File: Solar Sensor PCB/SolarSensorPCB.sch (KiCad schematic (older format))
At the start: 36 parts, among them J1 Arduino_Nano_Header, P1 BATT, P10 SERIAL, P2 BATT, P3 DIO, P4 LOGO1, P5 LOGO2, P6 PCB, P7 ENC, P8 AREF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

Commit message: Updated PCB. Not finished yet!
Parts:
- removed BT1: PP3, symbol device:Battery
- removed C2: 100u, REInnovationFootprint:C_1V7_TH, symbol device:CP1
- removed C3: 100n, matts_components:C1_wide_lg_pad, symbol device:C
- removed D1: 1N5819, REInnovationFootprint:TH_Diode_1, symbol device:D_Schottky
- removed DISP1: OLED_I2C, REInnovationFootprint:TH_OLED1306, symbol SolarSensorPCB-rescue:OLED_I2C-matts_components
- removed J1: Arduino_Nano_Header, REInnovationFootprint:NANO_DIP_30_600, symbol SolarSensorPCB-rescue:Arduino_Nano_Header-matts_components
- removed P1: BATT, symbol Connector_Generic:Conn_01x02
- removed P2: BATT, REInnovationFootprint:Batt_Connector_Strain_Relief, symbol Connector_Generic:Conn_01x02
- removed P3: DIO, matts_components:SIL-8_lg_pad_1mm, symbol Connector_Generic:Conn_01x08
- removed P8: AREF, matts_components:SIL-2_solder_connect, symbol Connector_Generic:Conn_01x02
- removed P9: AIO, matts_components:SIL-3_lg_pad_1mm, symbol Connector_Generic:Conn_01x03
- removed R2: 4K7, REInnovationFootprint:TH_Resistor_1, symbol device:R
- removed SW2: DOWN, REInnovationFootprint:SW_PUSH_SMALL_lg_pad, symbol SolarSensorPCB-rescue:SW_PUSH-matts_components
- removed SW3: SPST, REInnovationFootprint:SW_SPDT_R_Angle_ALIEX, symbol SolarSensorPCB-rescue:SPST-matts_components
- removed U1: DS18B20, matts_components:TO92-EBC_large_pad, symbol SolarSensorPCB-rescue:DS18B20-matts_components
- removed U2: MCP1702-50, matts_components:TO92_MC1703, symbol SolarSensorPCB-rescue:MCP1702-50-matts_components
- removed U?: TLC2252A, symbol device:Opamp_Dual_Generic
- removed U?: TLC2252A, symbol Device:Opamp_Dual_Generic
- added C4: 100n, REInnovationFootprint:SM_C_0805, symbol device:C
- added D1: LED, REInnovationFootprint:SM0805_LED, symbol device:LED
- added IC1: ATTINY85-P, REInnovationFootprint:SM_SOIC_8, symbol matts_components:ATTINY85-P
- added J1: ISP, REInnovationFootprint:ISP_3x2, symbol Connector_Generic:Conn_02x03_Odd_Even
- added J2: ADC, REInnovationFootprint:SIL-4_large_pad, symbol Connector_Generic:Conn_01x04
- added P1: I2C_OLED, REInnovationFootprint:SIL-4_large_pad, symbol Connector_Generic:Conn_01x04
- added R6: 330R, REInnovationFootprint:SM0805, symbol device:R
- added U1: TSV911xxLx, REInnovationFootprint:SM_SOT-23-5, symbol Amplifier_Operational:TSV911xxLx
- added U2: LM75B, REInnovationFootprint:SM_SOIC_8, symbol Sensor_Temperature:LM75B
- C1: footprint matts_components:C1_wide_lg_pad -> REInnovationFootprint:SM_C_0805
- C2, C3, C6: renamed from C?; footprint matts_components:C1_wide_lg_pad -> REInnovationFootprint:SM_C_0805
- C5: renamed from C?; footprint REInnovationFootprint:C_1V7_TH -> REInnovationFootprint:SM_4x5.3
- P10: footprint matts_components:SIL-4_Grove_SIL -> REInnovationFootprint:SIL-4_Grove_SCREW
- P6: footprint REInnovationFootprint:PCB_50x100mm_PP3_CutOut_EdgeCut -> REInnovationFootprint:PCB_50x50mm_PP3_Cutout
- R1, R2, R3, R5: renamed from R?; footprint (none) -> REInnovationFootprint:SM0805
- R4: value 100k -> 47k; footprint REInnovationFootprint:TH_Resistor_1 -> REInnovationFootprint:SM0805
- U3: renamed from U?; footprint (none) -> REInnovationFootprint:SM_MSOP10-0.5
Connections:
- net labels added: D0, D1, D2, D3, D4, IRR1+, IRR1-, SW1
- net labels removed: IRR, IRR+, IRR-, SW_DOWN, SW_UP, TEMP_DATA, VCC
- wire segments 163 -> 140
- no-connect marks 8 -> 5
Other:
- note added: "ATTiny85 Arduino Pins:\nIC Pin: Arduino Ref\n1 5/A0/RST\n2 3/A3\n3 4/A2\n4 GND\n5 0 - PWM\n6 1 - PWM\n7 2/A1\n8 +ve supply"
- note added: "I2C Pull Up"
- note added: "ISP Connections:\n1 - MISO\n2 - Vcc\n3 - SCLK\n4 - MOSI\n5 - Reset\n6 - GND"
- note added: "Irradiance sensor + amplifier"
- note added: "Potential OLED output for a little display?"
- note added: "Switch/LED combo for \ndata display and user input"
- note added: "We can measure two more \nanalog pins here, if needed."
- note removed: "Battery Supply. Switch on Batt Holder"
- moved on the sheet: C1, C2, C3, C5, C6, D2, P10, P4, P5, P6, P7, R1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

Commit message: Updated PCB v0.1
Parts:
- removed P4: LOGO1, CuriousElectric3:CEC_Globe_10mm_FCU, symbol Connector_Generic:Conn_01x01
- C1: JLCPCB Add (none) -> Y; JLCPCB Cost (none) -> 0.0105; LCSC (none) -> C107135
- C2, C3, C4, C6: JLCPCB Add (none) -> Y; JLCPCB Cost (none) -> 0.0108; LCSC (none) -> C49678
- C5: JLCPCB Add (none) -> Y; JLCPCB Cost (none) -> 0.0566; LCSC (none) -> C134722
- D1: JLCPCB Add (none) -> Y; JLCPCB Cost (none) -> 0.0135; LCSC (none) -> C2293
- P6: footprint REInnovationFootprint:PCB_50x50mm_PP3_Cutout -> REInnovationFootprint:PCB_40mm_Round
- R1: JLCPCB Add (none) -> Y; JLCPCB Cost (none) -> 0.0045; LCSC (none) -> C38522
- R2: JLCPCB Add (none) -> Y; JLCPCB Cost (none) -> 0.0045; LCSC (none) -> C17414
- R3: JLCPCB Add (none) -> Y; JLCPCB Cost (none) -> 0.0040; LCSC (none) -> C17414
- R4: JLCPCB Add (none) -> Y; JLCPCB Cost (none) -> 0.0040; LCSC (none) -> C17713
- R5: JLCPCB Add (none) -> Y; JLCPCB Cost (none) -> 0.0040; LCSC (none) -> C38522
- R6: JLCPCB Add (none) -> Y; JLCPCB Cost (none) -> 0.0050; LCSC (none) -> C237764
- SW1: footprint REInnovationFootprint:SW_PUSH_SMALL_lg_pad -> REInnovationFootprint:SMD_SW_6x3_5; JLCPCB Add (none) -> Y; JLCPCB Cost (none) -> 0.0391; LCSC (none) -> C319333
- U1: JLCPCB Add (none) -> Y; JLCPCB Cost (none) -> 0.4576; LCSC (none) -> C361052
- U2: JLCPCB Add (none) -> Y; JLCPCB Cost (none) -> 0.3457; LCSC (none) -> C34565
- U3: JLCPCB Add (none) -> Y; JLCPCB Cost (none) -> 4.7766; LCSC (none) -> C37593
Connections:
- net D0: now also P1.4 (Pin_4), U2.1 (SDA), U3.9 (SDA); no longer P1.3 (Pin_3), U2.2 (SCL), U3.10 (SCL)
- net D2: now also P1.3 (Pin_3), U2.2 (SCL), U3.10 (SCL); no longer P1.4 (Pin_4), U2.1 (SDA), U3.9 (SDA)
- net IRR1+: no longer names the net of C1.1, R4.1, U1.1, U3.4 (AIN0)
- no-connect marks 5 -> 4
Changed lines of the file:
@@
 F 0 "SW1" H 9550 4350 50  0000 C CNN
 F 1 "UP" H 9550 4100 50  0000 C CNN
-F 2 "REInnovationFootprint:SW_PUSH_SMALL_lg_pad" H 9550 4400 50  0001 C CNN
+F 2 "REInnovationFootprint:SMD_SW_6x3_5" H 9550 4400 50  0001 C CNN
 F 3 "" H 9550 4400 50  0000 C CNN
+F 4 "C319333" H 9550 4200 50  0001 C CNN "LCSC"
+F 5 "Y" H 9550 4200 50  0001 C CNN "JLCPCB Add"
+F 6 "0.0391" H 9550 4200 50  0001 C CNN "JLCPCB Cost"
 	1    9550 4200
 	1    0    0    -1
@@
 Text HLabel 7150 3650 2    60   Output ~ 0
 SCL_I2C
-Text HLabel 4450 4700 0    60   Input ~ 0
-IRR1+
 Text HLabel 7150 3800 2    60   Output ~ 0
 SDA_I2C
@@
 F 2 "REInnovationFootprint:SM0805" V 2280 3450 50  0001 C CNN
 F 3 "" H 2350 3450 50  0000 C CNN
+F 4 "C17713" H 2350 3450 50  0001 C CNN "LCSC"
+F 5 "Y" H 2350 3450 50  0001 C CNN "JLCPCB Add"
+F 6 "0.0040" H 2350 3450 50  0001 C CNN "JLCPCB Cost"
 	1    2350 3450
 	0    1    1    0
@@
 	-1   0    0    -1
 $EndComp
-Text HLabel 3250 2300 0    60   Input ~ 0
+Text HLabel 3250 2350 0    60   Input ~ 0
 Rx
-Text HLabel 3250 2400 0    60   Input ~ 0
+Text HLabel 3250 2450 0    60   Input ~ 0
 Tx
-Text HLabel 1500 2250 2    60   Input ~ 0
-Rx
-Text HLabel 1500 2150 2    60   Input ~ 0
-Tx
-Wire Wire Line
-	1500 2250 1250 2250
-Wire Wire Line
-	1500 2150 1250 2150
 Wire Wire Line
 	1750 2000 1750 2050
@@
 F 2 "REInnovationFootprint:SM_C_0805" H 2388 3000 50  0001 C CNN
 F 3 "" H 2350 3150 50  0000 C CNN
+F 4 "C107135" H 2350 3150 50  0001 C CNN "LCSC"
+F 5 "Y" H 2350 3150 50  0001 C CNN "JLCPCB Add"
+F 6 "0.0105" H 2350 3150 50  0001 C CNN "JLCPCB Cost"
 	1    2350 3150
 	0    1    1    0
-$EndComp
-$Comp
-L Connector_Generic:Conn_01x01 P4
-U 1 1 59012C98
-P 6650 6450
-F 0 "P4" H 6650 6550 50  0000 C CNN
-F 1 "LOGO1" V 6750 6450 50  0000 C CNN
-F 2 "CuriousElectric3:CEC_Globe_10mm_FCU" H 6650 6450 50  0001 C CNN
-F 3 "" H 6650 6450 50  0000 C CNN
-	1    6650 6450
-	1    0    0    -1
 $EndComp
 $Comp
@@
 F 0 "P6" H 6650 7150 50  0000 C CNN
 F 1 "PCB" V 6750 7050 50  0000 C CNN
-F 2 "REInnovationFootprint:PCB_50x50mm_PP3_Cutout" H 6650 7050 50  0001 C CNN
+F 2 "REInnovationFootprint:PCB_40mm_Round" H 6650 7050 50  0001 C CNN
 F 3 "" H 6650 7050 50  0000 C CNN
 	1    6650 7050
@@
 	1    0    0    -1
 $EndComp
-NoConn ~ 6450 6450
 NoConn ~ 6450 6750
 NoConn ~ 6450 7050
-NoConn ~ 6500 7400
+NoConn ~ 6450 7400
 Text Notes 5500 4550 0    60   ~ 0
 16 Bit ADC
@@
 F 2 "REInnovationFootprint:SM_4x5.3" H 10250 2250 50  0001 C CNN
 F 3 "" H 10250 2250 50  0000 C CNN
+F 4 "C134722" H 10250 2250 50  0001 C CNN "LCSC"
+F 5 "Y" H 10250 2250 50  0001 C CNN "JLCPCB Add"
+F 6 "0.0566" H 10250 2250 50  0001 C CNN "JLCPCB Cost"
 	1    10250 2250
 	1    0    0    -1
@@
 F 2 "REInnovationFootprint:SM_C_0805" H 10588 2100 50  0001 C CNN
 F 3 "" H 10550 2250 50  0000 C CNN
+F 4 "C49678" H 10550 2250 50  0001 C CNN "LCSC"
+F 5 "Y" H 10550 2250 50  0001 C CNN "JLCPCB Add"
+F 6 "0.0108" H 10550 2250 50  0001 C CNN "JLCPCB Cost"
 	1    10550 2250
 	1    0    0    -1
@@
 F 2 "REInnovationFootprint:SM_MSOP10-0.5" H 5950 3700 60  0001 C CNN
 F 3 "" H 5950 3700 60  0000 C CNN
+F 4 "C37593" H 5750 3800 50  0001 C CNN "LCSC"
+F 5 "Y" H 5750 3800 50  0001 C CNN "JLCPCB Add"
+F 6 "4.7766" H 5750 3800 50  0001 C CNN "JLCPCB Cost"
 	1    5750 3800
 	1    0    0    -1
@@
 F 2 "REInnovationFootprint:SM0805" V 4830 3550 50  0001 C CNN
 F 3 "~" H 4900 3550 50  0001 C CNN
+F 4 "C17414" H 4900 3550 50  0001 C CNN "LCSC"
+F 5 "Y" H 4900 3550 50  0001 C CNN "JLCPCB Add"
+F 6 "0.0040" H 4900 3550 50  0001 C CNN "JLCPCB Cost"
 	1    4900 3550
 	1    0    0    -1
@@
 F 2 "REInnovationFootprint:SM_C_0805" H 4638 3750 50  0001 C CNN
 F 3 "" H 4600 3900 50  0000 C CNN
+F 4 "C49678" H 4600 3900 50  0001 C CNN "LCSC"
+F 5 "Y" H 4600 3900 50  0001 C CNN "JLCPCB Add"
+F 6 "0.0108" H 4600 3900 50  0001 C CNN "JLCPCB Cost"
 	1    4600 3900
 	1    0    0    -1
@@
 F 2 "REInnovationFootprint:SM0805" V 3680 1700 50  0001 C CNN
 F 3 "~" H 3750 1700 50  0001 C CNN
+F 4 "C38522" H 3750 1700 50  0001 C CNN "LCSC"
+F 5 "Y" H 3750 1700 50  0001 C CNN "JLCPCB Add"
+F 6 "0.0045" H 3750 1700 50  0001 C CNN "JLCPCB Cost"
 	1    3750 1700
 	1    0    0    -1
@@
 F 2 "REInnovationFootprint:SM0805" V 3980 1700 50  0001 C CNN
 F 3 "~" H 4050 1700 50  0001 C CNN
+F 4 "C17414" H 4050 1700 50  0001 C CNN "LCSC"
+F 5 "Y" H 4050 1700 50  0001 C CNN "JLCPCB Add"
+F 6 "0.0045" H 4050 1700 50  0001 C CNN "JLCPCB Cost"
 	1    4050 1700
 	1    0    0    -1
@@
 F 2 "REInnovationFootprint:SM0805" V 5130 3450 50  0001 C CNN
 F 3 "~" H 5200 3450 50  0001 C CNN
+F 4 "C38522" H 5200 3450 50  0001 C CNN "LCSC"
+F 5 "Y" H 5200 3450 50  0001 C CNN "JLCPCB Add"
+F 6 "0.0040" H 5200 3450 50  0001 C CNN "JLCPCB Cost"
 	1    5200 3450
 	1    0    0    -1
@@
 Wire Wire Line
 	5400 3100 5400 3150
-Text HLabel 4450 4850 0    60   Input ~ 0
-IRR1-
-Wire Wire Line
-	4450 4700 5300 4700
 Wire Wire Line
 	5300 4700 5300 4100
@@
 Wire Wire Line
 	5350 4250 5350 4850
-Wire Wire Line
-	5350 4850 4450 4850
-Text HLabel 3300 4600 2    60   Output ~ 0
-IRR1-
-Text HLabel 3300 4250 2    60   Output ~ 0
-IRR1+
 $Comp
 L device:C C2
@@
 F 2 "REInnovationFootprint:SM_C_0805" H 2738 5050 50  0001 C CNN
 F 3 "" H 2700 5200 50  0000 C CNN
+F 4 "C49678" H 2700 5200 50  0001 C CNN "LCSC"
+F 5 "Y" H 2700 5200 50  0001 C CNN "JLCPCB Add"
+F 6 "0.0108" H 2700 5200 50  0001 C CNN "JLCPCB Cost"
 	1    2700 5200
 	-1   0    0    1
@@
 L power:GND #PWR09
 U 1 1 60E3C134
-P 3100 4600
-F 0 "#PWR09" H 3100 4350 50  0001 C CNN
-F 1 "GND" H 3100 4450 50  0000 C CNN
-F 2 "" H 3100 4600 50  0000 C CNN
-F 3 "" H 3100 4600 50  0000 C CNN
-	1    3100 4600
-	1    0    0    -1
-$EndComp
-Wire Wire Line
-	3100 4600 3300 4600
-Wire Wire Line
-	2850 4250 3300 4250
+P 3500 4850
+F 0 "#PWR09" H 3500 4600 50  0001 C CNN
+F 1 "GND" H 3500 4700 50  0000 C CNN
+F 2 "" H 3500 4850 50  0000 C CNN
+F 3 "" H 3500 4850 50  0000 C CNN
+	1    3500 4850
+	1    0    0    -1
+$EndComp
 Connection ~ 2850 4250
 $Comp
@@
 	5600 2000 6950 2000
 Connection ~ 6950 2000
+Text HLabel 3250 2200 0    60   Input ~ 0
+SCL_I2C
 Text HLabel 3250 2000 0    60   Input ~ 0
-SCL_I2C
-Text HLabel 3250 2200 0    60   Input ~ 0
 SDA_I2C
 $Comp
@@
 F 2 "REInnovationFootprint:SM0805" V 9130 3400 50  0001 C CNN
 F 3 "~" H 9200 3400 50  0001 C CNN
+F 4 "C237764" H 9200 3400 50  0001 C CNN "LCSC"
+F 5 "Y" H 9200 3400 50  0001 C CNN "JLCPCB Add"
+F 6 "0.0050" H 9200 3400 50  0001 C CNN "JLCPCB Cost"
 	1    9200 3400
 	1    0    0    -1
@@
 F 2 "REInnovationFootprint:SM0805_LED" H 9200 3800 50  0001 C CNN
 F 3 "~" H 9200 3800 50  0001 C CNN
+F 4 "C2293" H 9200 3800 50  0001 C CNN "LCSC"
+F 5 "Y" H 9200 3800 50  0001 C CNN "JLCPCB Add"
+F 6 "0.0135" H 9200 3800 50  0001 C CNN "JLCPCB Cost"
 	1    9200 3800
 	0    -1   -1   0
@@
 F 2 "REInnovationFootprint:SM_SOT-23-5" H 2300 4050 50  0001 L CNN
 F 3 "www.st.com/resource/en/datasheet/tsv911.pdf" H 2400 4450 50  0001 C CNN
+F 4 "C361052" H 2400 4250 50  0001 C CNN "LCSC"
+F 5 "Y" H 2400 4250 50  0001 C CNN "JLCPCB Add"
+F 6 "0.4576" H 2400 4250 50  0001 C CNN "JLCPCB Cost"
 	1    2400 4250
 	1    0    0    -1
@@
 F 2 "REInnovationFootprint:SM_SOIC_8" H 4350 6600 50  0001 C CNN
 F 3 "http://www.ti.com/lit/ds/symlink/lm75b.pdf" H 4350 6600 50  0001 C CNN
+F 4 "C34565" H 4350 6600 50  0001 C CNN "LCSC"
+F 5 "Y" H 4350 6600 50  0001 C CNN "JLCPCB Add"
+F 6 "0.3457" H 4350 6600 50  0001 C CNN "JLCPCB Cost"
 	1    4350 6600
 	1    0    0    -1
@@
 F 2 "REInnovationFootprint:SM_C_0805" H 5338 6400 50  0001 C CNN
 F 3 "" H 5300 6550 50  0000 C CNN
+F 4 "C49678" H 5300 6550 50  0001 C CNN "LCSC"
+F 5 "Y" H 5300 6550 50  0001 C CNN "JLCPCB Add"
+F 6 "0.0108" H 5300 6550 50  0001 C CNN "JLCPCB Cost"
 	1    5300 6550
 	-1   0    0    1
@@
 Wire Wire Line
 	9150 5350 9850 5350
-Wire Wire Line
-	3250 2400 5600 2400
 Connection ~ 5600 2400
-Wire Wire Line
-	5600 2300 3250 2300
 Connection ~ 5600 2300
 Wire Wire Line
@@
 Text Notes 6100 5200 0    60   ~ 0
 We can measure two more \nanalog pins here, if needed.
+Wire Wire Line
+	2250 2150 2250 2400
+Wire Wire Line
+	1250 2150 2250 2150
+Wire Wire Line
+	2250 2400 3300 2400
+Wire Wire Line
+	1450 2300 1450 2250
+Wire Wire Line
+	1450 2300 3300 2300
+Wire Wire Line
+	1450 2250 1250 2250
+Wire Wire Line
+	3250 2350 3300 2350
+Wire Wire Line
+	3300 2350 3300 2300
+Connection ~ 3300 2300
+Wire Wire Line
+	3300 2300 5600 2300
+Wire Wire Line
+	3250 2450 3300 2450
+Wire Wire Line
+	3300 2450 3300 2400
+Connection ~ 3300 2400
+Wire Wire Line
+	3300 2400 5600 2400
+Wire Wire Line
+	3500 4850 5350 4850
+Wire Wire Line
+	3850 4250 3850 4700
+Wire Wire Line
+	3850 4700 5300 4700
+Wire Wire Line
+	2850 4250 3850 4250
 $EndSCHEMATC

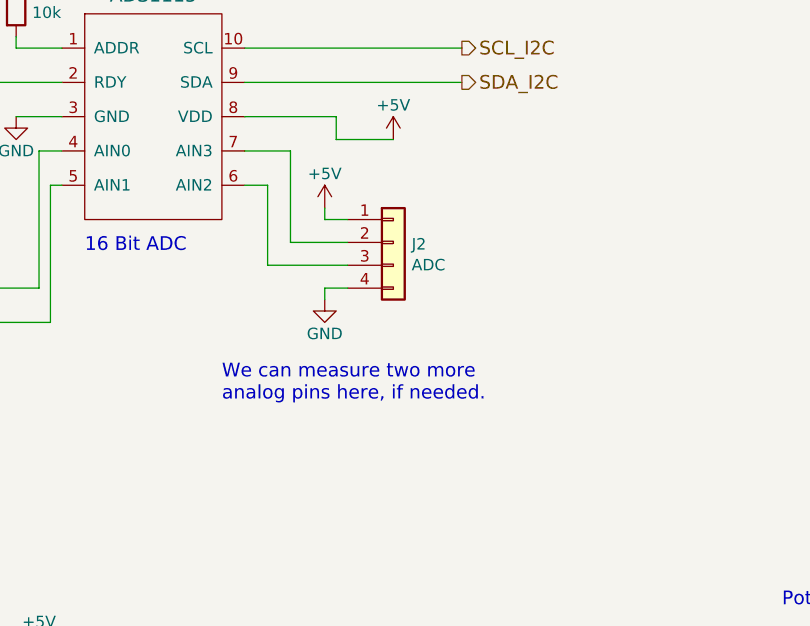
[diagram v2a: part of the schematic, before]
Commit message: Updated firmware. Updated PCB
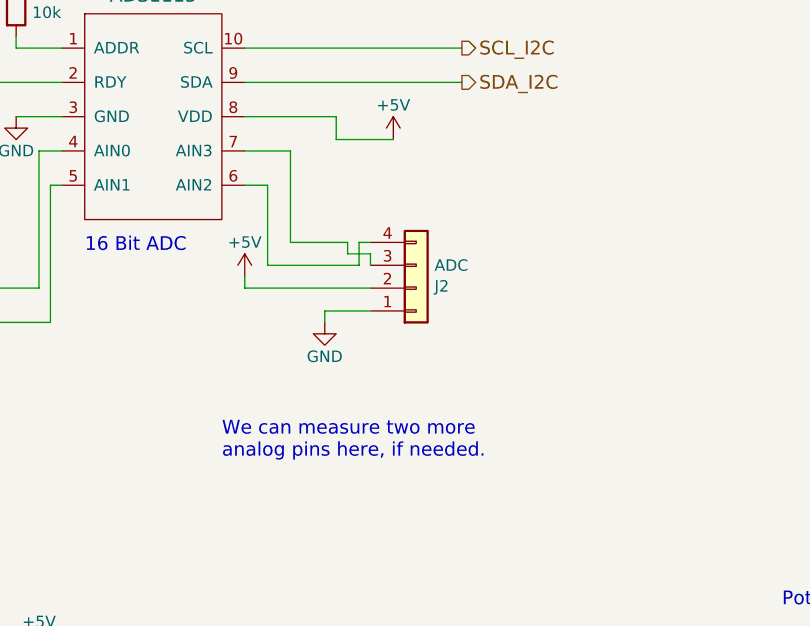
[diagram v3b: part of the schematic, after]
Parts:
- P6: footprint REInnovationFootprint:PCB_40mm_Round -> REInnovationFootprint:PCB_40mm_Round_SolarSensorPCB_design
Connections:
- net +5V: now also J2.2 (Pin_2); no longer J2.1 (Pin_1)
- net GND: now also J2.1 (Pin_1); no longer J2.4 (Pin_4)
- net at U3.6 (AIN2): now also J2.4 (Pin_4); no longer J2.3 (Pin_3)
- net at U3.7 (AIN3): now also J2.3 (Pin_3); no longer J2.2 (Pin_2)
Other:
- moved on the sheet: J2
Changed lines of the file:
@@
 F 0 "P6" H 6650 7150 50  0000 C CNN
 F 1 "PCB" V 6750 7050 50  0000 C CNN
-F 2 "REInnovationFootprint:PCB_40mm_Round" H 6650 7050 50  0001 C CNN
+F 2 "REInnovationFootprint:PCB_40mm_Round_SolarSensorPCB_design" H 6650 7050 50  0001 C CNN
 F 3 "" H 6650 7050 50  0000 C CNN
 	1    6650 7050
@@
 L Connector_Generic:Conn_01x04 J2
 U 1 1 60E3FE6C
-P 6850 4500
-F 0 "J2" H 6930 4492 50  0000 L CNN
-F 1 "ADC" H 6930 4401 50  0000 L CNN
-F 2 "REInnovationFootprint:SIL-4_large_pad" H 6850 4500 50  0001 C CNN
-F 3 "~" H 6850 4500 50  0001 C CNN
-	1    6850 4500
-	1    0    0    -1
+P 6950 4700
+F 0 "J2" H 7030 4692 50  0000 L CNN
+F 1 "ADC" H 7030 4601 50  0000 L CNN
+F 2 "REInnovationFootprint:SIL-4_large_pad" H 6950 4700 50  0001 C CNN
+F 3 "~" H 6950 4700 50  0001 C CNN
+	1    6950 4700
+	1    0    0    1
 $EndComp
 $Comp
 L power:+5V #PWR025
 U 1 1 60E40773
-P 6550 4350
-F 0 "#PWR025" H 6550 4200 50  0001 C CNN
-F 1 "+5V" H 6550 4500 50  0000 C CNN
-F 2 "" H 6550 4350 50  0000 C CNN
-F 3 "" H 6550 4350 50  0000 C CNN
-	1    6550 4350
+P 6200 4650
+F 0 "#PWR025" H 6200 4500 50  0001 C CNN
+F 1 "+5V" H 6200 4800 50  0000 C CNN
+F 2 "" H 6200 4650 50  0000 C CNN
+F 3 "" H 6200 4650 50  0000 C CNN
+	1    6200 4650
 	1    0    0    -1
 $EndComp
@@
 L power:GND #PWR026
 U 1 1 60E40BB0
-P 6550 4750
-F 0 "#PWR026" H 6550 4500 50  0001 C CNN
-F 1 "GND" H 6550 4600 50  0000 C CNN
-F 2 "" H 6550 4750 50  0000 C CNN
-F 3 "" H 6550 4750 50  0000 C CNN
-	1    6550 4750
-	1    0    0    -1
-$EndComp
-Wire Wire Line
-	6650 4700 6550 4700
-Wire Wire Line
-	6550 4700 6550 4750
-Wire Wire Line
-	6550 4350 6550 4400
-Wire Wire Line
-	6550 4400 6650 4400
+P 6550 4850
+F 0 "#PWR026" H 6550 4600 50  0001 C CNN
+F 1 "GND" H 6550 4700 50  0000 C CNN
+F 2 "" H 6550 4850 50  0000 C CNN
+F 3 "" H 6550 4850 50  0000 C CNN
+	1    6550 4850
+	1    0    0    -1
+$EndComp
+Wire Wire Line
+	6550 4800 6550 4850
+Wire Wire Line
+	6200 4650 6200 4700
 Wire Wire Line
 	6650 4500 6400 4500
@@
 Wire Wire Line
 	6300 4250 6300 4600
-Wire Wire Line
-	6300 4600 6650 4600
 $Comp
 L Sensor_Temperature:LM75B U2
@@
 Text Notes 8800 4650 0    60   ~ 0
 Switch/LED combo for \ndata display and user input
-Text Notes 6100 5200 0    60   ~ 0
+Text Notes 6100 5450 0    60   ~ 0
 We can measure two more \nanalog pins here, if needed.
 Wire Wire Line
@@
 Wire Wire Line
 	2850 4250 3850 4250
+Wire Wire Line
+	6700 4600 6700 4500
+Wire Wire Line
+	6700 4500 6750 4500
+Wire Wire Line
+	6300 4600 6700 4600
+Wire Wire Line
+	6650 4500 6650 4550
+Wire Wire Line
+	6650 4550 6750 4550
+Wire Wire Line
+	6750 4550 6750 4600
+Wire Wire Line
+	6200 4700 6750 4700
+Wire Wire Line
+	6550 4800 6750 4800
 $EndSCHEMATC

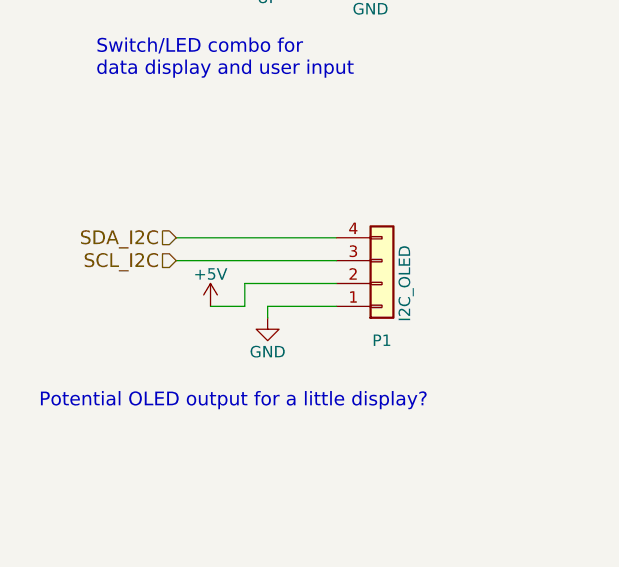
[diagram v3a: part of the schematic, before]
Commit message: big update of PCB
Changed from ATTiny85 to ATmega328
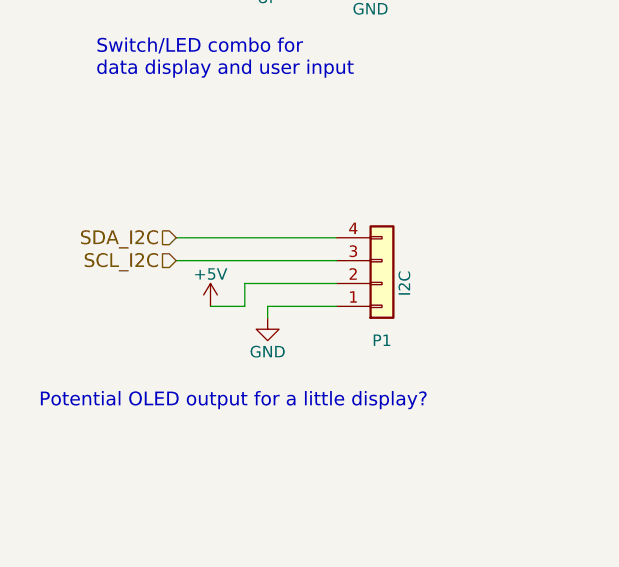
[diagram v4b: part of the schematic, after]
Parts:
- P1: value I2C_OLED -> I2C
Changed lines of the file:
@@
 P 10050 5550
 F 0 "P1" H 10050 5800 50  0000 C CNN
-F 1 "I2C_OLED" V 10150 5550 50  0000 C CNN
+F 1 "I2C" V 10150 5550 50  0000 C CNN
 F 2 "REInnovationFootprint:SIL-4_large_pad" H 10050 5550 50  0001 C CNN
 F 3 "" H 10050 5550 50  0000 C CNN
